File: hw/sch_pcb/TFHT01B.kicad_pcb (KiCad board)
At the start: 2 copper layers, 30 x 15 mm, 31 parts, among them J1 SM04B-GHS-TB, J2 SM04B-GHS-TB, M1 M3, M2 M3, M3 M3, M4 M3, M5 M3, M6 M3, M7 CAP-SF2, Q1 BC817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

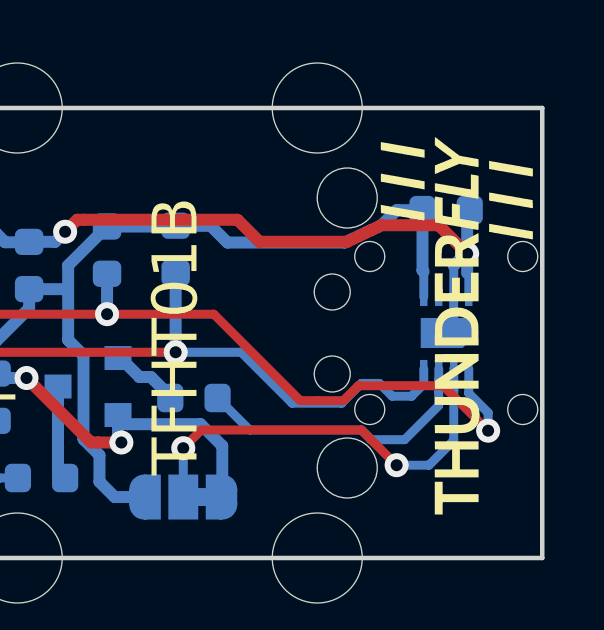
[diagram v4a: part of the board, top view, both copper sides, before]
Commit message: Resolve DRC errors.
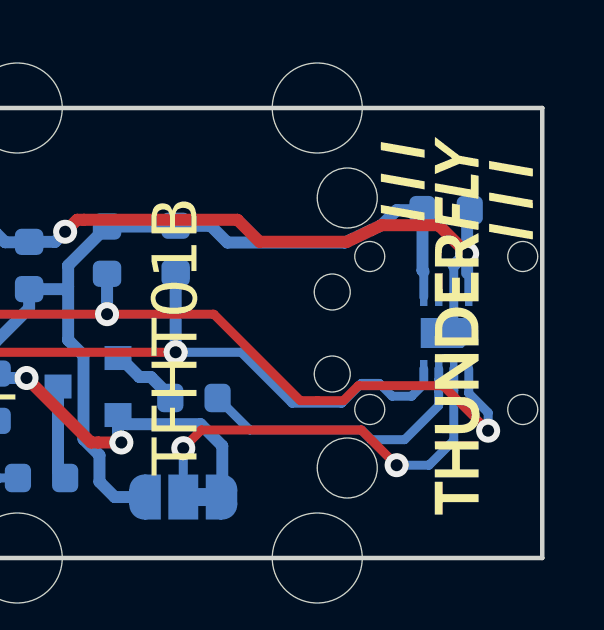
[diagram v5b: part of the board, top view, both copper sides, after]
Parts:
- JP1: value SolderJumper_3_Bridged12 -> Address select
- U1: value SHT31-DIS-B -> SHT35A-DIS
